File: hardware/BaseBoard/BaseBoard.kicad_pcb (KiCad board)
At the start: 2 copper layers, 81.3 x 106.7 mm, 109 parts, among them IC1 PCF8574RGTR, J1-ESP1 ESP-1-L, J1-ESP2 ESP-1-L, J1-ESP3 ESP-1-L, J1-ESP4 ESP-1-L, J1-ESP5 ESP-1-L, J1-ESP6 ESP-1-L, J1-ESP7 ESP-1-L, J1-ESP8 ESP-1-L, J2-ESP1 ESP-1-R, J2-ESP2 ESP-1-R, J2-ESP3 ESP-1-R, J2-ESP4 ESP-1-R, J2-ESP5 ESP-1-R, J2-ESP6 ESP-1-R, J2-ESP7 ESP-1-R, J2-ESP8 ESP-1-R, J3-BUS1 BUS-IN, J3-BUS2 BUS-IN, J3-BUS3 BUS-IN, J3-BUS4 BUS-IN, J3-BUS5 BUS-IN, J3-BUS6 BUS-IN, J3-BUS7 BUS-IN, J3-BUS8 BUS-IN, J4-BUS1 BUS-OUT, J4-BUS2 BUS-OUT, J4-BUS3 BUS-OUT, J4-BUS4 BUS-OUT, J4-BUS5 BUS-OUT, J4-BUS6 BUS-OUT, J4-BUS7 BUS-OUT, J4-BUS8 BUS-OUT, Q1 AO3401A, Q2 AO3401A, Q3 AO3401A, Q4 AO3401A, Q5 AO3401A, Q6 AO3401A, Q7 AO3401A, Q8 AO3401A, SW1 SW_DIP_SPSTx03

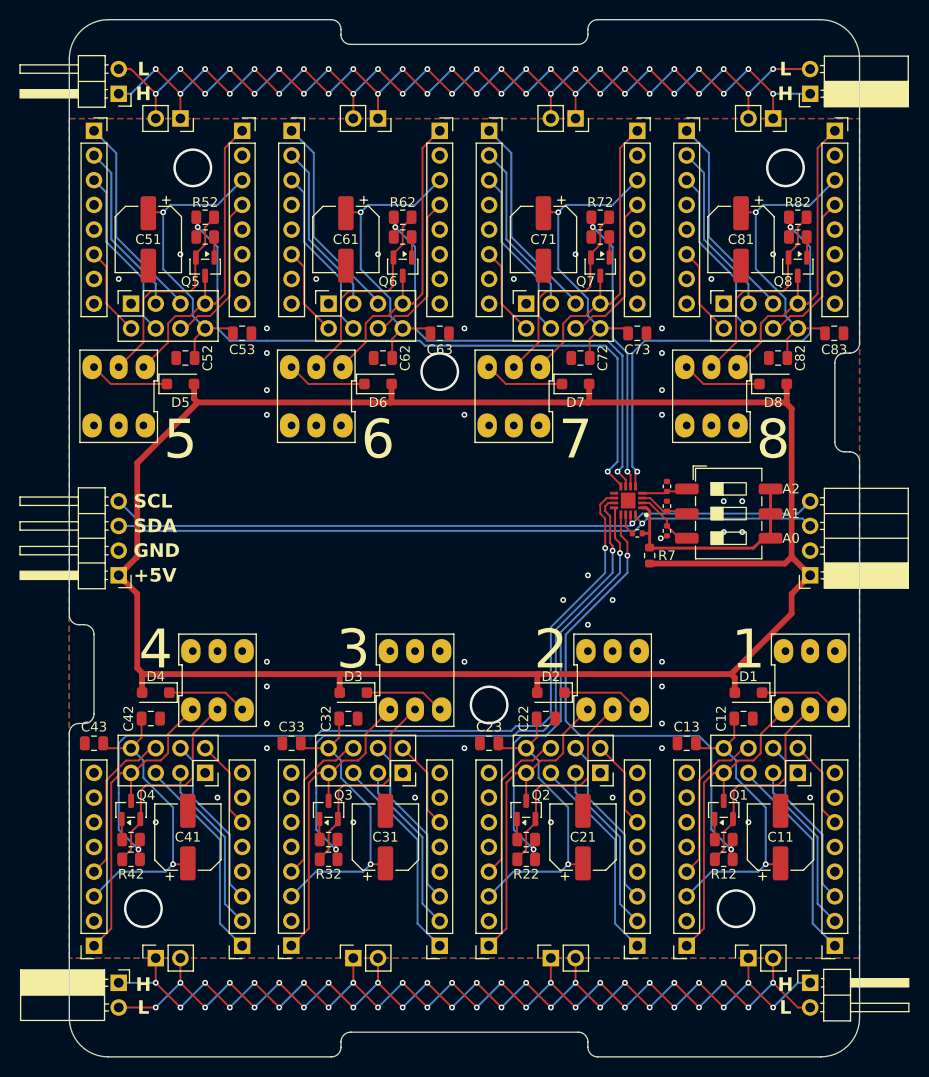
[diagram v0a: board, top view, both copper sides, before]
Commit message: Updated BaseBoard to kicad v10.
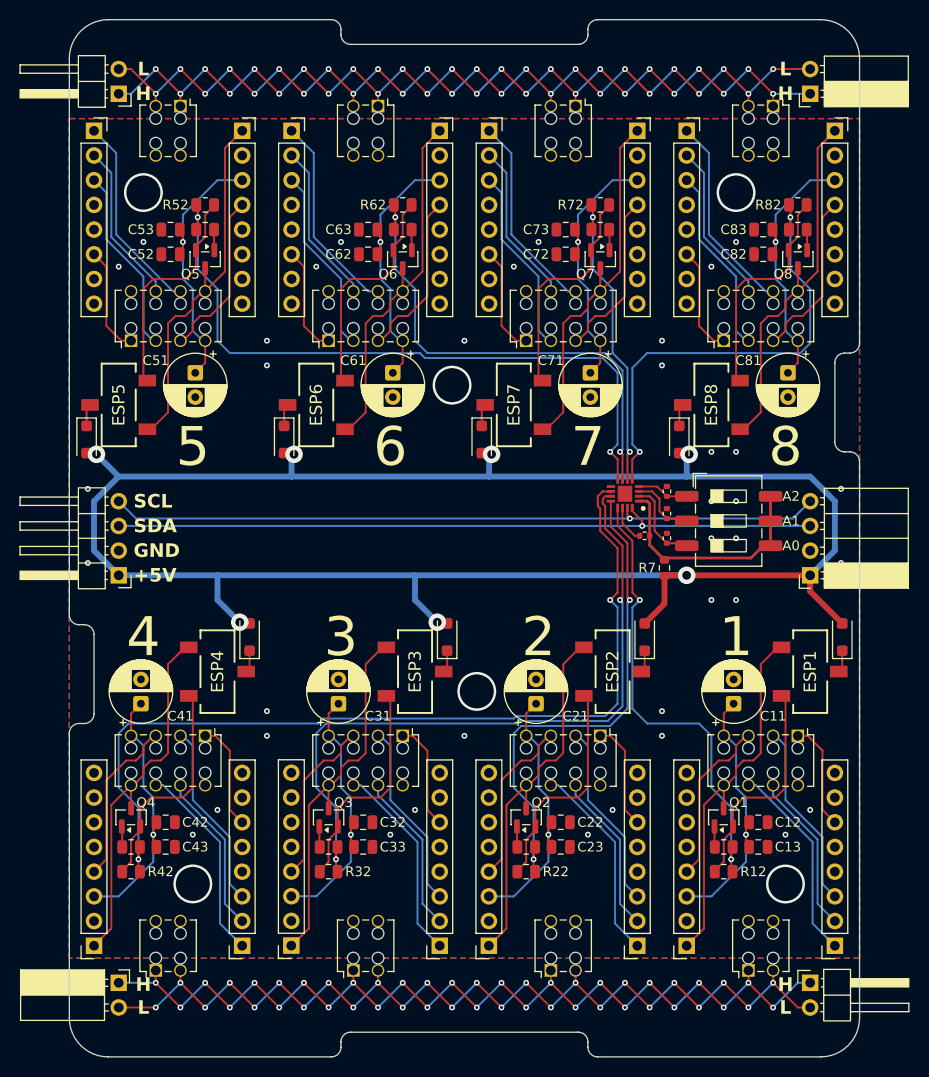
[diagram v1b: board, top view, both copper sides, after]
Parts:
- C11, C21, C31, C41, C51, C61, C71, C81: footprint Capacitor_SMD:CP_Elec_6.3x7.7 -> Capacitor_THT:CP_Radial_D6.3mm_P2.50mm
- ESP1, ESP2, ESP3, ESP4, ESP5, ESP6, ESP7, ESP8: footprint sw_dpdt_xlx:SW_DPDT_XLX -> LIB_CL-SB-12B-01T:CLSB12B01T
- J3-BUS1, J3-BUS2, J3-BUS3, J3-BUS4, J3-BUS5, J3-BUS6, J3-BUS7, J3-BUS8: footprint Connector_PinSocket_2.54mm:PinSocket_2x04_P2.54mm_Vertical -> Connector_Wuerth:Wuerth_WR-PHD_61300825721_Standard_2x04_P2.54mm_Vertical
- J4-BUS1, J4-BUS2, J4-BUS3, J4-BUS4, J4-BUS5, J4-BUS6, J4-BUS7, J4-BUS8: footprint Connector_PinSocket_2.54mm:PinSocket_1x02_P2.54mm_Vertical -> Connector_Wuerth:Wuerth_WR-PHD_61300425721_Standard_2x02_P2.54mm_Vertical
- R7: value 50 -> 47
- moved C71 14.5 mm to (175.5, 55.4)
- moved C21 14.5 mm to (169.9, 89.4)
- moved C51 14.5 mm to (134.9, 55.4)
- moved C61 14.5 mm to (155.2, 55.4)
- moved C81 14.5 mm to (195.8, 55.4)
- moved C11 14.5 mm to (190.2, 89.4)
- moved C31 14.5 mm to (149.6, 89.4)
- moved C41 14.5 mm to (129.3, 89.4)
- moved C13 13.0 mm to (192.8, 104.1), turned to 180 degrees
- moved C23 13.0 mm to (172.5, 104.1), turned to 180 degrees
- moved C63 13.0 mm to (152.7, 40.6), turned to 0 degrees
- moved C73 13.0 mm to (173.0, 40.6), turned to 0 degrees
- moved C43 13.0 mm to (131.8, 104.1), turned to 180 degrees
- moved C33 13.0 mm to (152.1, 104.1), turned to 180 degrees
- moved C53 13.0 mm to (132.3, 40.6), turned to 0 degrees
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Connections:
- ESP1 pad 1: Net-(J2-ESP1-Pin_1) -> Net-(ESP1-A)
- ESP1 pad 2: Net-(Q1-S) -> Net-(D1-K)
- ESP1 pad 3: Net-(D1-K) -> Net-(ESP1-C)
- ESP2 pad 1: Net-(J2-ESP2-Pin_1) -> Net-(ESP2-A)
- ESP2 pad 2: Net-(Q2-S) -> Net-(D2-K)
- ESP2 pad 3: Net-(D2-K) -> Net-(ESP2-C)
- ESP3 pad 1: Net-(J2-ESP3-Pin_1) -> Net-(ESP3-A)
- ESP3 pad 2: Net-(Q3-S) -> Net-(D3-K)
- ESP3 pad 3: Net-(D3-K) -> Net-(ESP3-C)
- ESP4 pad 1: Net-(J2-ESP4-Pin_1) -> Net-(ESP4-A)
- ESP4 pad 2: Net-(Q4-S) -> Net-(D4-K)
- ESP4 pad 3: Net-(D4-K) -> Net-(ESP4-C)
- ESP5 pad 1: Net-(J2-ESP5-Pin_1) -> Net-(ESP5-A)
- ESP5 pad 2: Net-(Q5-S) -> Net-(D5-K)
- ESP5 pad 3: Net-(D5-K) -> Net-(ESP5-C)
- ESP6 pad 1: Net-(J2-ESP6-Pin_1) -> Net-(ESP6-A)
- ESP6 pad 2: Net-(Q6-S) -> Net-(D6-K)
- ESP6 pad 3: Net-(D6-K) -> Net-(ESP6-C)
- ESP7 pad 1: Net-(J2-ESP7-Pin_1) -> Net-(ESP7-A)
- ESP7 pad 2: Net-(Q7-S) -> Net-(D7-K)
- ESP7 pad 3: Net-(D7-K) -> Net-(ESP7-C)
- ESP8 pad 1: Net-(J2-ESP8-Pin_1) -> Net-(ESP8-A)
- ESP8 pad 2: Net-(Q8-S) -> Net-(D8-K)
- ESP8 pad 3: Net-(D8-K) -> Net-(ESP8-C)
- J2-ESP1 pad 1: Net-(J2-ESP1-Pin_1) -> Net-(ESP1-A)
- J2-ESP2 pad 1: Net-(J2-ESP2-Pin_1) -> Net-(ESP2-A)
- J2-ESP3 pad 1: Net-(J2-ESP3-Pin_1) -> Net-(ESP3-A)
- J2-ESP4 pad 1: Net-(J2-ESP4-Pin_1) -> Net-(ESP4-A)
- J2-ESP5 pad 1: Net-(J2-ESP5-Pin_1) -> Net-(ESP5-A)
- J2-ESP6 pad 1: Net-(J2-ESP6-Pin_1) -> Net-(ESP6-A)
- J2-ESP7 pad 1: Net-(J2-ESP7-Pin_1) -> Net-(ESP7-A)
- J2-ESP8 pad 1: Net-(J2-ESP8-Pin_1) -> Net-(ESP8-A)
- J3-BUS1 pad 1: GNDREF -> Net-(J1-ESP1-Pin_6)
- J3-BUS1 pad 2: Net-(J1-ESP1-Pin_6) -> GNDREF
- J3-BUS1 pad 3: Net-(J1-ESP1-Pin_2) -> Net-(J1-ESP1-Pin_3)
- J3-BUS1 pad 4: Net-(J1-ESP1-Pin_3) -> Net-(J1-ESP1-Pin_2)
- J3-BUS1 pad 5: Net-(J1-ESP1-Pin_1) -> Net-(J2-ESP1-Pin_4)
- J3-BUS1 pad 6: Net-(J2-ESP1-Pin_4) -> Net-(J1-ESP1-Pin_1)
- J3-BUS1 pad 7: Net-(J2-ESP1-Pin_1) -> +3V3-ESP1
- J3-BUS1 pad 8: +3V3-ESP1 -> Net-(ESP1-A)
- J3-BUS2 pad 1: GNDREF -> Net-(J1-ESP2-Pin_6)
- J3-BUS2 pad 2: Net-(J1-ESP2-Pin_6) -> GNDREF
- J3-BUS2 pad 3: Net-(J1-ESP2-Pin_2) -> Net-(J1-ESP2-Pin_3)
- J3-BUS2 pad 4: Net-(J1-ESP2-Pin_3) -> Net-(J1-ESP2-Pin_2)
- J3-BUS2 pad 5: Net-(J1-ESP2-Pin_1) -> Net-(J2-ESP2-Pin_4)
- J3-BUS2 pad 6: Net-(J2-ESP2-Pin_4) -> Net-(J1-ESP2-Pin_1)
- J3-BUS2 pad 7: Net-(J2-ESP2-Pin_1) -> +3V3-ESP2
- J3-BUS2 pad 8: +3V3-ESP2 -> Net-(ESP2-A)
- J3-BUS3 pad 1: GNDREF -> Net-(J1-ESP3-Pin_6)
- J3-BUS3 pad 2: Net-(J1-ESP3-Pin_6) -> GNDREF
- J3-BUS3 pad 3: Net-(J1-ESP3-Pin_2) -> Net-(J1-ESP3-Pin_3)
- J3-BUS3 pad 4: Net-(J1-ESP3-Pin_3) -> Net-(J1-ESP3-Pin_2)
- J3-BUS3 pad 5: Net-(J1-ESP3-Pin_1) -> Net-(J2-ESP3-Pin_4)
- J3-BUS3 pad 6: Net-(J2-ESP3-Pin_4) -> Net-(J1-ESP3-Pin_1)
- J3-BUS3 pad 7: Net-(J2-ESP3-Pin_1) -> +3V3-ESP3
- J3-BUS3 pad 8: +3V3-ESP3 -> Net-(ESP3-A)
- J3-BUS4 pad 1: GNDREF -> Net-(J1-ESP4-Pin_6)
- J3-BUS4 pad 2: Net-(J1-ESP4-Pin_6) -> GNDREF
- J3-BUS4 pad 3: Net-(J1-ESP4-Pin_2) -> Net-(J1-ESP4-Pin_3)
- J3-BUS4 pad 4: Net-(J1-ESP4-Pin_3) -> Net-(J1-ESP4-Pin_2)
- J3-BUS4 pad 5: Net-(J1-ESP4-Pin_1) -> Net-(J2-ESP4-Pin_4)
- J3-BUS4 pad 6: Net-(J2-ESP4-Pin_4) -> Net-(J1-ESP4-Pin_1)
- J3-BUS4 pad 7: Net-(J2-ESP4-Pin_1) -> +3V3-ESP4
- J3-BUS4 pad 8: +3V3-ESP4 -> Net-(ESP4-A)
- J3-BUS5 pad 1: GNDREF -> Net-(J1-ESP5-Pin_6)
- J3-BUS5 pad 2: Net-(J1-ESP5-Pin_6) -> GNDREF
- J3-BUS5 pad 3: Net-(J1-ESP5-Pin_2) -> Net-(J1-ESP5-Pin_3)
- J3-BUS5 pad 4: Net-(J1-ESP5-Pin_3) -> Net-(J1-ESP5-Pin_2)
- J3-BUS5 pad 5: Net-(J1-ESP5-Pin_1) -> Net-(J2-ESP5-Pin_4)
- J3-BUS5 pad 6: Net-(J2-ESP5-Pin_4) -> Net-(J1-ESP5-Pin_1)
- J3-BUS5 pad 7: Net-(J2-ESP5-Pin_1) -> +3V3-ESP5
- J3-BUS5 pad 8: +3V3-ESP5 -> Net-(ESP5-A)
- J3-BUS6 pad 1: GNDREF -> Net-(J1-ESP6-Pin_6)
- J3-BUS6 pad 2: Net-(J1-ESP6-Pin_6) -> GNDREF
- J3-BUS6 pad 3: Net-(J1-ESP6-Pin_2) -> Net-(J1-ESP6-Pin_3)
- J3-BUS6 pad 4: Net-(J1-ESP6-Pin_3) -> Net-(J1-ESP6-Pin_2)
- J3-BUS6 pad 5: Net-(J1-ESP6-Pin_1) -> Net-(J2-ESP6-Pin_4)
- J3-BUS6 pad 6: Net-(J2-ESP6-Pin_4) -> Net-(J1-ESP6-Pin_1)
- J3-BUS6 pad 7: Net-(J2-ESP6-Pin_1) -> +3V3-ESP6
- J3-BUS6 pad 8: +3V3-ESP6 -> Net-(ESP6-A)
- J3-BUS7 pad 1: GNDREF -> Net-(J1-ESP7-Pin_6)
- J3-BUS7 pad 2: Net-(J1-ESP7-Pin_6) -> GNDREF
- J3-BUS7 pad 3: Net-(J1-ESP7-Pin_2) -> Net-(J1-ESP7-Pin_3)
- J3-BUS7 pad 4: Net-(J1-ESP7-Pin_3) -> Net-(J1-ESP7-Pin_2)
- J3-BUS7 pad 5: Net-(J1-ESP7-Pin_1) -> Net-(J2-ESP7-Pin_4)
- J3-BUS7 pad 6: Net-(J2-ESP7-Pin_4) -> Net-(J1-ESP7-Pin_1)
- J3-BUS7 pad 7: Net-(J2-ESP7-Pin_1) -> +3V3-ESP7
- J3-BUS7 pad 8: +3V3-ESP7 -> Net-(ESP7-A)
- J3-BUS8 pad 1: GNDREF -> Net-(J1-ESP8-Pin_6)
- J3-BUS8 pad 2: Net-(J1-ESP8-Pin_6) -> GNDREF
- J3-BUS8 pad 3: Net-(J1-ESP8-Pin_2) -> Net-(J1-ESP8-Pin_3)
- J3-BUS8 pad 4: Net-(J1-ESP8-Pin_3) -> Net-(J1-ESP8-Pin_2)
- J3-BUS8 pad 5: Net-(J1-ESP8-Pin_1) -> Net-(J2-ESP8-Pin_4)
- J3-BUS8 pad 6: Net-(J2-ESP8-Pin_4) -> Net-(J1-ESP8-Pin_1)
- J3-BUS8 pad 7: Net-(J2-ESP8-Pin_1) -> +3V3-ESP8
- J3-BUS8 pad 8: +3V3-ESP8 -> Net-(ESP8-A)
- J4-BUS1 pad 2: BUS1_L -> unconnected-(J4-BUS1-Pin_2-Pad2)
- J4-BUS2 pad 2: BUS1_L -> unconnected-(J4-BUS2-Pin_2-Pad2)
- J4-BUS3 pad 2: BUS1_L -> unconnected-(J4-BUS3-Pin_2-Pad2)
- J4-BUS4 pad 2: BUS1_L -> unconnected-(J4-BUS4-Pin_2-Pad2)
- J4-BUS5 pad 2: BUS2_L -> unconnected-(J4-BUS5-Pin_2-Pad2)
- J4-BUS6 pad 2: BUS2_L -> unconnected-(J4-BUS6-Pin_2-Pad2)
- J4-BUS7 pad 2: BUS2_L -> unconnected-(J4-BUS7-Pin_2-Pad2)
- J4-BUS8 pad 2: BUS2_L -> unconnected-(J4-BUS8-Pin_2-Pad2)
- Q1 pad 2: Net-(Q1-S) -> Net-(ESP1-C)
- Q1 pad 3: Net-(J2-ESP1-Pin_1) -> Net-(ESP1-A)
- Q2 pad 2: Net-(Q2-S) -> Net-(ESP2-C)
- Q2 pad 3: Net-(J2-ESP2-Pin_1) -> Net-(ESP2-A)
- Q3 pad 2: Net-(Q3-S) -> Net-(ESP3-C)
- Q3 pad 3: Net-(J2-ESP3-Pin_1) -> Net-(ESP3-A)
- Q4 pad 2: Net-(Q4-S) -> Net-(ESP4-C)
- Q4 pad 3: Net-(J2-ESP4-Pin_1) -> Net-(ESP4-A)
- Q5 pad 2: Net-(Q5-S) -> Net-(ESP5-C)
- Q5 pad 3: Net-(J2-ESP5-Pin_1) -> Net-(ESP5-A)
- Q6 pad 2: Net-(Q6-S) -> Net-(ESP6-C)
- Q6 pad 3: Net-(J2-ESP6-Pin_1) -> Net-(ESP6-A)
- Q7 pad 2: Net-(Q7-S) -> Net-(ESP7-C)
- Q7 pad 3: Net-(J2-ESP7-Pin_1) -> Net-(ESP7-A)
- Q8 pad 2: Net-(Q8-S) -> Net-(ESP8-C)
- Q8 pad 3: Net-(J2-ESP8-Pin_1) -> Net-(ESP8-A)
- R12 pad 1: Net-(Q1-S) -> Net-(ESP1-C)
- R22 pad 1: Net-(Q2-S) -> Net-(ESP2-C)
- R32 pad 1: Net-(Q3-S) -> Net-(ESP3-C)
- R42 pad 1: Net-(Q4-S) -> Net-(ESP4-C)
- R52 pad 1: Net-(Q5-S) -> Net-(ESP5-C)
- R62 pad 1: Net-(Q6-S) -> Net-(ESP6-C)
- R72 pad 1: Net-(Q7-S) -> Net-(ESP7-C)
- R82 pad 1: Net-(Q8-S) -> Net-(ESP8-C)
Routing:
- net Net-(ESP4-A): track 0.00 -> 38.1 mm
- net Net-(ESP8-A): track 0.00 -> 38.1 mm
- net Net-(ESP6-A): track 0.00 -> 38.1 mm
- net Net-(ESP5-A): track 0.00 -> 38.1 mm
- net Net-(ESP1-A): track 0.00 -> 38.1 mm
- net Net-(ESP2-A): track 0.00 -> 38.1 mm
- net Net-(ESP7-A): track 0.00 -> 38.1 mm
- net Net-(ESP3-A): track 0.00 -> 38.1 mm
- net Net-(J2-ESP1-Pin_1): track 33.0 -> 0.00 mm
- net Net-(J2-ESP4-Pin_1): track 33.0 -> 0.00 mm
- net Net-(J2-ESP2-Pin_1): track 33.0 -> 0.00 mm
- net Net-(J2-ESP8-Pin_1): track 33.0 -> 0.00 mm
- net Net-(J2-ESP6-Pin_1): track 33.0 -> 0.00 mm
- net Net-(J2-ESP5-Pin_1): track 33.0 -> 0.00 mm
- net Net-(J2-ESP3-Pin_1): track 33.0 -> 0.00 mm
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
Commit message: Minor imrpovements in positions and footprints.
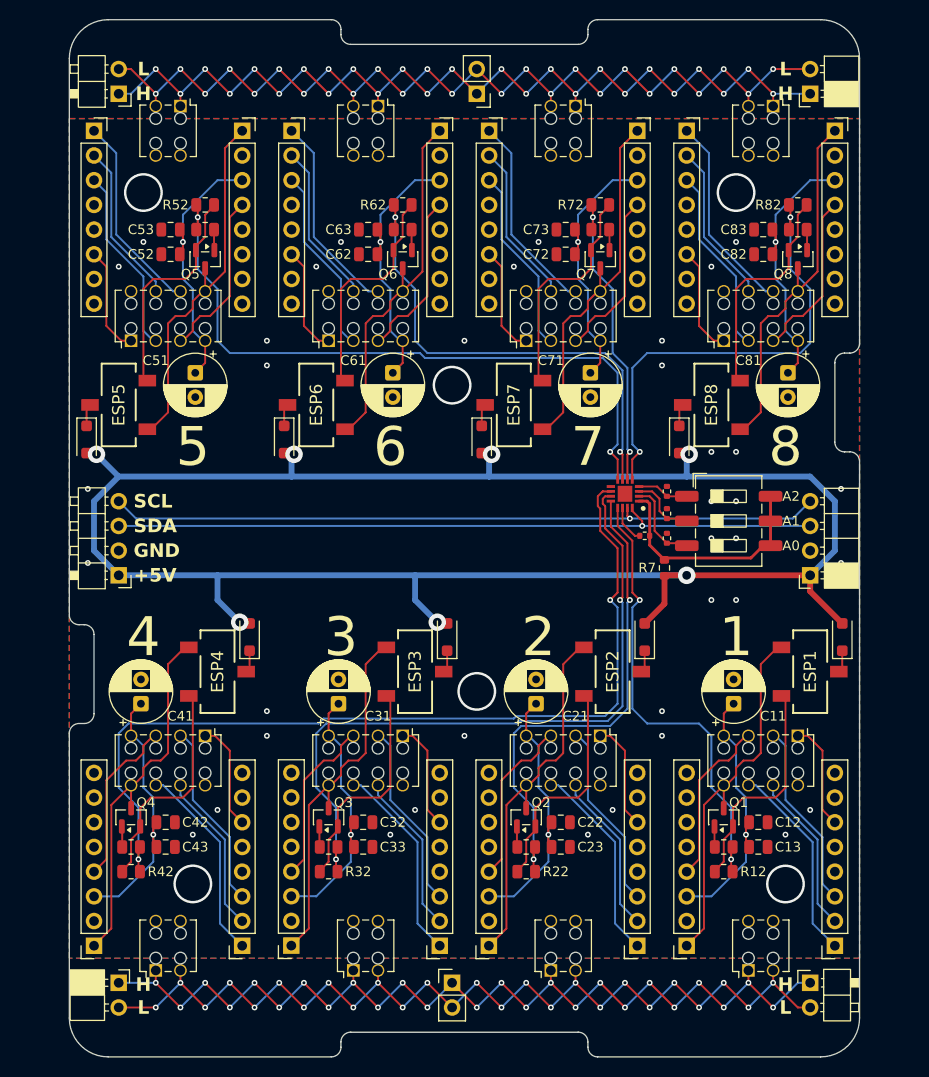
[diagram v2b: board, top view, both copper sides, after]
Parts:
- added BUS_TAP1: Conn_01x02_Socket, Connector_PinHeader_2.54mm:PinHeader_1x02_P2.54mm_Vertical, F.Cu at (161.3, 118.1)
- added BUS_TAP2: Conn_01x02_Socket, Connector_PinHeader_2.54mm:PinHeader_1x02_P2.54mm_Vertical, F.Cu at (163.8, 26.7)
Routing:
- net BUS2_L: vias 26 -> 25
- net BUS2_H: vias 26 -> 25
- net BUS1_L: vias 26 -> 25
- net BUS1_H: vias 26 -> 25
